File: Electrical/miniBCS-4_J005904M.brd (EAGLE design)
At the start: 146.1 x 146.1 mm, 173 parts, among them IC1 WIZ850io, J11 QWIIC_RIGHT_ANGLE, J14 A0/A1, J2 1734035-2, M2 TEENSY4.1, U1 ADA4084, U10 MAX11300GCM, U11 CAT811, U2 2G17, U3 ISL23425, U4 AD9833, U5 ISO1H815G, U6 78L12, U7 ADM3312/5, U8 2G17, U9 79L12, X1 OSC-OE-CFPS-9

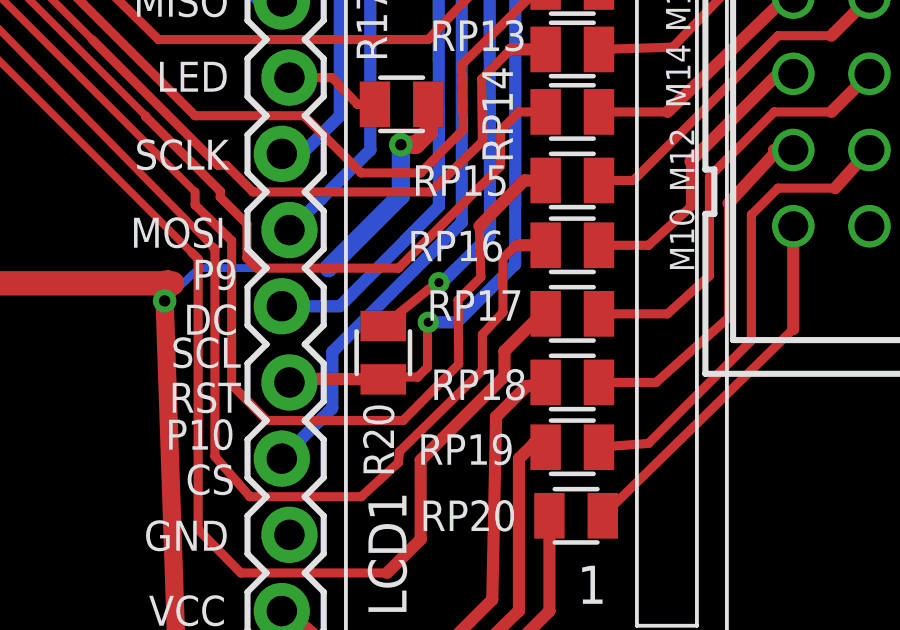
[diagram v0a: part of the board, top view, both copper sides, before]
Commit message: Updated BOM, PCB files, example, and laser cut file
Add QWIIC and SPI connector cutouts to laser file
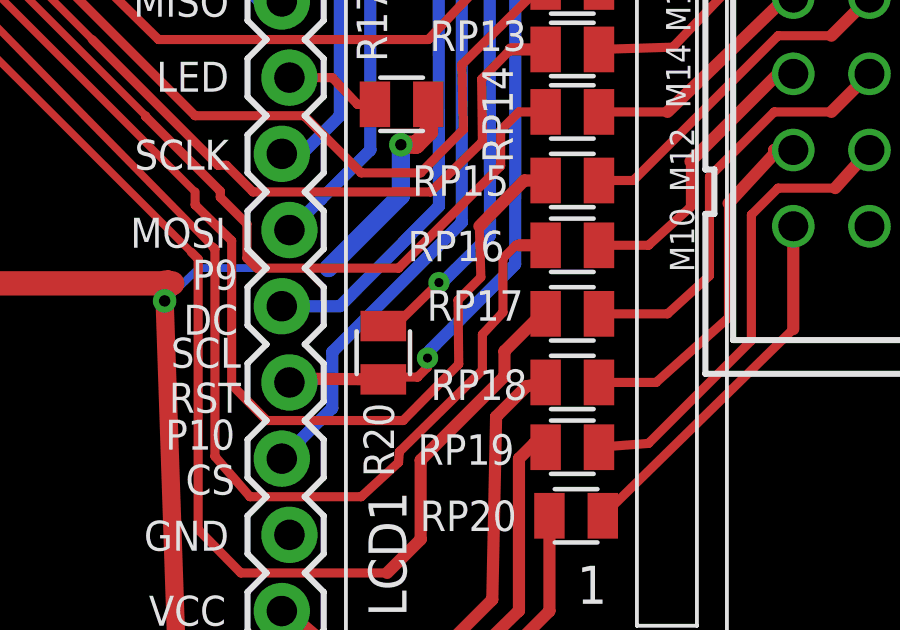
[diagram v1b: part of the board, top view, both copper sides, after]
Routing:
- net !TFTRST: track 67.6 -> 67.0 mm
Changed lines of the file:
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@@
 <grid distance="1" unitdist="mil" unit="mil" style="lines" multiple="1" display="yes" altdistance="0.025" altunitdist="inch" altunit="inch"/>
 <layers>
-<layer number="1" name="Top" color="12" fill="1" visible="no" active="yes"/>
+<layer number="1" name="Top" color="12" fill="1" visible="yes" active="yes"/>
 <layer number="2" name="Route2" color="1" fill="3" visible="no" active="no"/>
 <layer number="3" name="Route3" color="4" fill="3" visible="no" active="no"/>
@@
 <layer number="14" name="Route14" color="1" fill="6" visible="no" active="no"/>
 <layer number="15" name="Route15" color="4" fill="6" visible="no" active="no"/>
-<layer number="16" name="Bottom" color="1" fill="1" visible="no" active="yes"/>
+<layer number="16" name="Bottom" color="1" fill="1" visible="yes" active="yes"/>
 <layer number="17" name="Pads" color="2" fill="1" visible="yes" active="yes"/>
-<layer number="18" name="Vias" color="2" fill="1" visible="no" active="yes"/>
-<layer number="19" name="Unrouted" color="12" fill="1" visible="no" active="yes"/>
+<layer number="18" name="Vias" color="2" fill="1" visible="yes" active="yes"/>
+<layer number="19" name="Unrouted" color="12" fill="1" visible="yes" active="yes"/>
 <layer number="20" name="Dimension" color="15" fill="1" visible="yes" active="yes"/>
 <layer number="21" name="tPlace" color="15" fill="1" visible="yes" active="yes"/>
-<layer number="22" name="bPlace" color="7" fill="1" visible="no" active="yes"/>
+<layer number="22" name="bPlace" color="7" fill="1" visible="yes" active="yes"/>
 <layer number="23" name="tOrigins" color="3" fill="1" visible="yes" active="yes"/>
-<layer number="24" name="bOrigins" color="15" fill="1" visible="no" active="yes"/>
-<layer number="25" name="tNames" color="15" fill="1" visible="no" active="yes"/>
-<layer number="26" name="bNames" color="7" fill="1" visible="no" active="yes"/>
+<layer number="24" name="bOrigins" color="15" fill="1" visible="yes" active="yes"/>
+<layer number="25" name="tNames" color="15" fill="1" visible="yes" active="yes"/>
+<layer number="26" name="bNames" color="7" fill="1" visible="yes" active="yes"/>
 <layer number="27" name="tValues" color="7" fill="1" visible="no" active="yes"/>
 <layer number="28" name="bValues" color="7" fill="1" visible="no" active="yes"/>
@@
 <wire x1="114.935" y1="63.6524" x2="119.507" y2="63.627" width="0.6096" layer="1"/>
 <wire x1="119.507" y1="63.627" x2="120.777" y2="64.897" width="0.6096" layer="1"/>
-<wire x1="106.426" y1="42.6974" x2="106.0704" y2="42.4688" width="0.3048" layer="1"/>
-<wire x1="106.0704" y1="42.4688" x2="104.5718" y2="41.2496" width="0.3048" layer="1"/>
+<wire x1="106.426" y1="42.6974" x2="105.0798" y2="41.3766" width="0.3048" layer="1"/>
+<wire x1="105.0798" y1="41.3766" x2="104.5718" y2="41.2496" width="0.3048" layer="1"/>
 <wire x1="94.488" y1="109.093" x2="101.0666" y2="109.093" width="0.6096" layer="16"/>
 <wire x1="101.0666" y1="109.093" x2="101.092" y2="109.1184" width="0.6096" layer="16"/>
@@
 <contactref element="M2" pad="37"/>
 <contactref element="R20" pad="2"/>
-<via x="106.0704" y="41.3766" extent="1-16" drill="0.3048"/>
-<wire x1="106.0704" y1="41.3766" x2="107.0356" y2="41.3766" width="0.4064" layer="16"/>
-<wire x1="107.0356" y1="41.3766" x2="108.966" y2="43.307" width="0.4064" layer="16"/>
+<via x="106.045" y="40.1828" extent="1-16" drill="0.3048"/>
+<wire x1="106.045" y1="40.1828" x2="106.1212" y2="40.4368" width="0.4064" layer="16"/>
+<wire x1="106.1212" y1="40.4368" x2="108.966" y2="43.307" width="0.4064" layer="16"/>
 <wire x1="108.966" y1="43.307" x2="108.9914" y2="66.0146" width="0.4064" layer="16"/>
 <wire x1="108.9914" y1="66.0146" x2="111.8362" y2="68.834" width="0.4064" layer="16"/>
@@
 <wire x1="111.125" y1="89.408" x2="111.125" y2="94.996" width="0.4064" layer="1"/>
 <wire x1="111.125" y1="94.996" x2="109.728" y2="96.393" width="0.4064" layer="1"/>
-<wire x1="106.0704" y1="41.3766" x2="106.045" y2="41.1734" width="0.3048" layer="1"/>
-<wire x1="106.045" y1="41.1734" x2="106.045" y2="39.878" width="0.3048" layer="1"/>
+<wire x1="106.045" y1="40.1828" x2="106.045" y2="39.878" width="0.3048" layer="1"/>
 <wire x1="106.045" y1="39.878" x2="105.7148" y2="39.5478" width="0.3048" layer="1"/>
 <wire x1="105.7148" y1="39.5478" x2="104.9274" y2="39.5478" width="0.3048" layer="1"/>
